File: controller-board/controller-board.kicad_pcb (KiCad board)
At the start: 2 copper layers, 130 x 115 mm, 152 parts, among them J1 Conn_01x02, J2 Conn_01x02, J3 Conn_01x02, J4 Conn_01x02, J5 Conn_01x03, J6 Conn_01x02, U1 CAT4201, U10 CAT4201, U11 CAT4201, U12 CAT4201, U13 CAT4201, U14 CAT4201, U15 CAT4201, U16 DGD0216, U2 PocketBeagle, U3 LTC3624, U4 CAT4201, U5 CAT4201, U6 CAT4201, U7 MCP4728, U8 ADS1015IRUGR, U9 ADS1015IRUGR

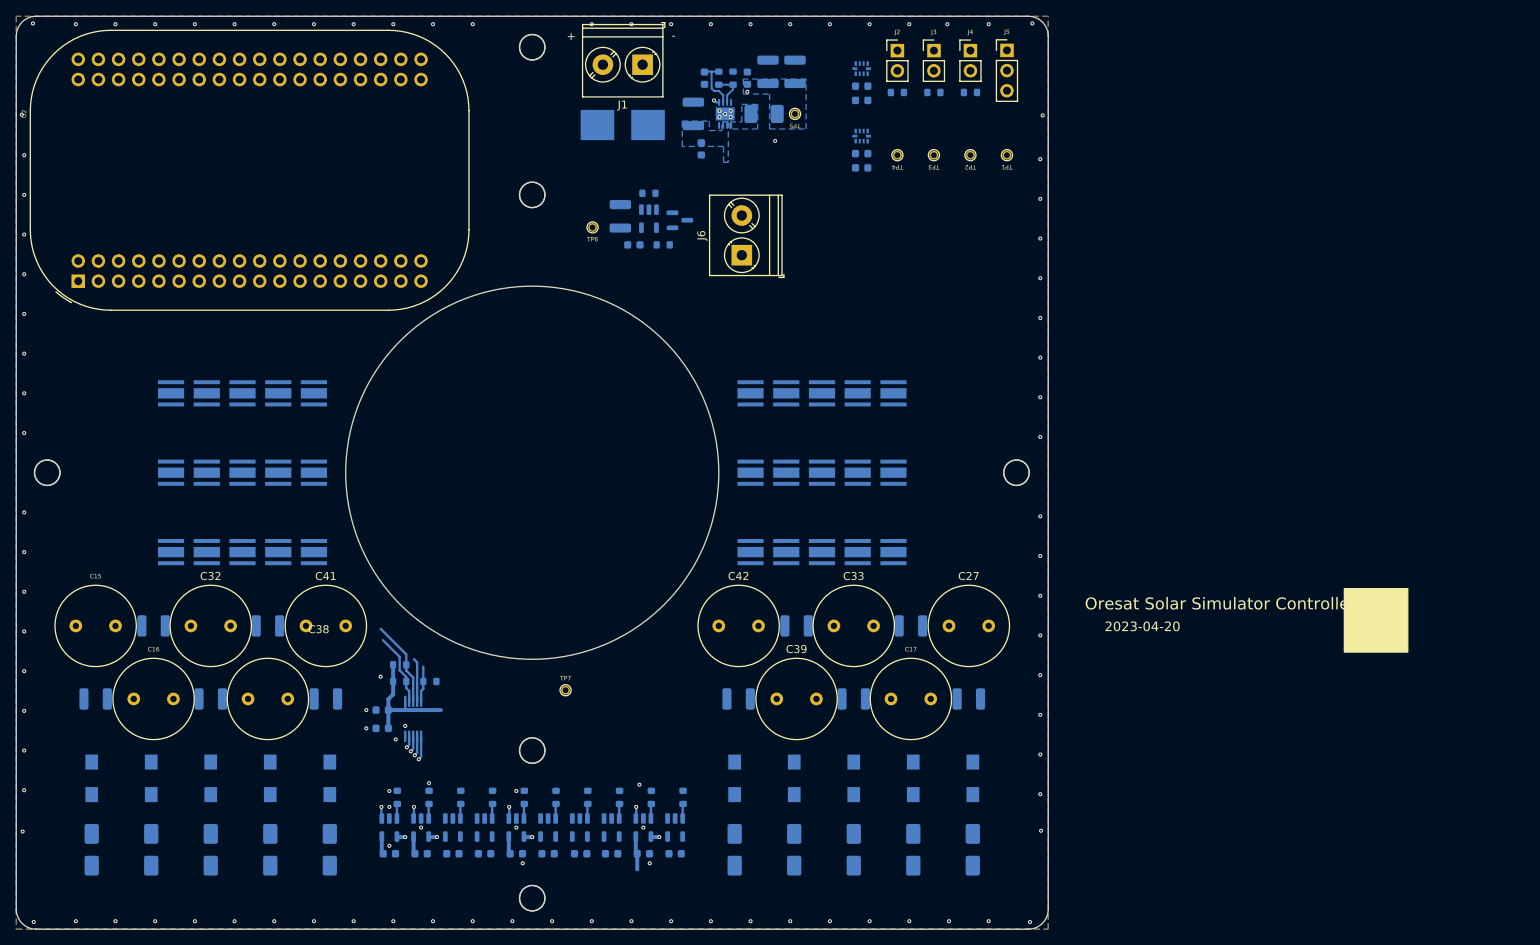
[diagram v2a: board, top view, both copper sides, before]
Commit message: Updated board design/layout and added step file
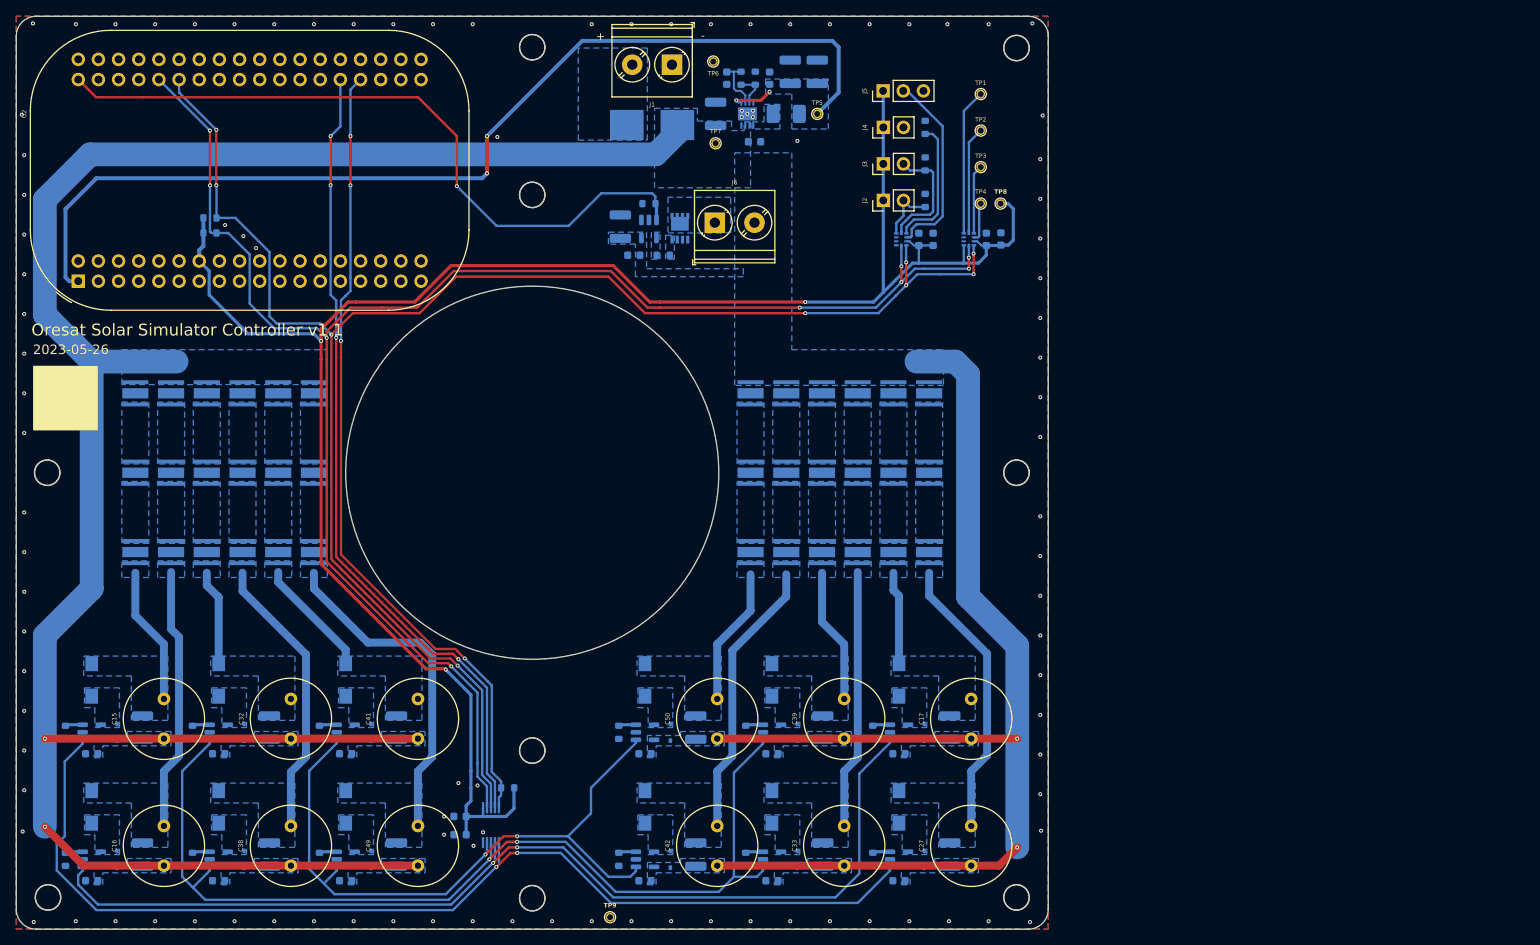
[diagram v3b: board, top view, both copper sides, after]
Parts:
- added C45: 4.7u, Capacitor_SMD:C_0603_1608Metric, B.Cu at (121.5, 153.9)
- added C46: 4.7u, Capacitor_SMD:C_0603_1608Metric, B.Cu at (159.2, 137.9)
- added C47: 22u, Capacitor_SMD:C_1210_3225Metric, B.Cu at (127.9, 150.6)
- added C48: 22u, Capacitor_SMD:C_1210_3225Metric, B.Cu at (165.6, 134.6)
- added C49: NP, Capacitor_THT:C_Radial_D10.0mm_H16.0mm_P5.00mm, F.Cu at (130.6, 152.0)
- added C50: NP, Capacitor_THT:C_Radial_D10.0mm_H16.0mm_P5.00mm, F.Cu at (168.3, 136.0)
- added D24: NSR0320, Diode_SMD:D_SOD-323, B.Cu at (124.7, 151.2)
- added D42: NSR0320, Diode_SMD:D_SOD-323, B.Cu at (162.4, 135.2)
- added D43: XPEBBL-L1-0000-00201, oresat-diodes:Cree-LED, B.Cu at (117.5, 92.5)
- added D44: XPEBBL-L1-0000-00201, oresat-diodes:Cree-LED, B.Cu at (117.5, 112.5)
- added D45: XPEBBL-L1-0000-00201, oresat-diodes:Cree-LED, B.Cu at (172.5, 92.5)
- added D46: XPEBBL-L1-0000-00201, oresat-diodes:Cree-LED, B.Cu at (172.5, 112.5)
- added D47: XPEBBL-L1-0000-00201, oresat-diodes:Cree-LED, B.Cu at (117.5, 102.5)
- added D48: XPEBBL-L1-0000-00201, oresat-diodes:Cree-LED, B.Cu at (172.5, 102.5)
- added L12: 56u, Inductor_SMD:L_Wuerth_HCI-5040, B.Cu at (121.5, 144.6)
- added L13: 56u, Inductor_SMD:L_Wuerth_HCI-5040, B.Cu at (159.2, 128.6)
- added R21: 10k, Resistor_SMD:R_0603_1608Metric, B.Cu at (118.2, 151.2)
- added R22: 10k, Resistor_SMD:R_0603_1608Metric, B.Cu at (155.9, 135.2)
- added REF**: MountingHole_3.2mm_M3, MountingHole:MountingHole_3.2mm_M3, F.Cu at (206.0, 49.0)
- added REF**: MountingHole_3.2mm_M3, MountingHole:MountingHole_3.2mm_M3, F.Cu at (84.0, 156.0)
- added REF**: MountingHole_3.2mm_M3, MountingHole:MountingHole_3.2mm_M3, F.Cu at (206.0, 156.0)
- added TP8: TestPoint-MinTH, oresat-misc:TestPoint-MinTH, F.Cu at (204.0, 68.6)
- added TP9: TestPoint-MinTH, oresat-misc:TestPoint-MinTH, F.Cu at (154.8, 158.5)
- added U17: CAT4201, Package_TO_SOT_SMD:TSOT-23-5, B.Cu at (121.5, 151.2)
- added U18: CAT4201, Package_TO_SOT_SMD:TSOT-23-5, B.Cu at (159.2, 135.2)
- D1, D15, D16, D17, D2, D3, D34, D35, D4, D7: value SS210A -> NSR0320; footprint Diode_SMD:D_SMA -> Diode_SMD:D_SOD-323
- D10, D11, D12, D13, D14, D18, D19, D20, D21, D22, D23, D25, D26, D27, D28, D29, D30, D31, D32, D33, D36, D37, D38, D39, D40, D41, D5, D6, D8, D9: footprint LED_SMD:LED_Cree-XP -> oresat-diodes:Cree-LED
- Q1: value ~ -> SQS460EN; footprint Package_TO_SOT_SMD:SOT-23 -> Package_SO:Vishay_PowerPAK_1212-8_Single
- moved TP7 71.4 mm to (168.1, 61.0)
- moved R13 61.3 mm to (104.4, 72.3)
- moved R12 61.2 mm to (104.4, 70.4)
- moved R3 46.5 mm to (86.2, 151.2), turned to -90 degrees
- moved R2 42.6 mm to (86.2, 135.2), turned to -90 degrees
- moved U4 41.7 mm to (89.5, 151.2), turned to 0 degrees
- moved C2 41.6 mm to (89.5, 153.9), turned to 180 degrees
- moved C11 39.6 mm to (89.5, 137.9), turned to 180 degrees
- moved U1 39.4 mm to (89.5, 135.2), turned to 0 degrees
- moved R18 38.6 mm to (102.2, 151.2), turned to -90 degrees
- moved R16 34.8 mm to (102.2, 135.2), turned to -90 degrees
- moved C3 34.6 mm to (191.2, 137.9), turned to 180 degrees
- moved U5 34.4 mm to (191.2, 135.2), turned to 0 degrees
- moved U13 33.7 mm to (105.5, 151.2), turned to 0 degrees
- moved C34 33.7 mm to (105.5, 153.9), turned to 180 degrees
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- renumbered U16 to Q2
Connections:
- Q1 pad 1: Net-(Q1-G) -> GND
- Q1 pad 3: Net-(J6-Pin_1) -> GND
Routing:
- net VCC: track 10.2 -> 420.6 mm, vias 0 -> 4
- net +3.3V: track 16.0 -> 247.7 mm, vias 0 -> 3
- net /SCL1: track 9.07 -> 210.9 mm, vias 0 -> 9
- net /SDA1: track 10.8 -> 210.7 mm, vias 0 -> 9
- net +5V: track 0.75 -> 134.6 mm, vias 2 -> 4
- net /RED_LIM: track 4.51 -> 135.8 mm
- net /GREEN_LIM: track 5.49 -> 129.9 mm, vias 3 -> 2
- net /BLUE_LIM: track 2.02 -> 124.7 mm, vias 1 -> 2
- net /DAC_RDY/~{BSY}: track 4.49 -> 102.7 mm, vias 0 -> 4
- net /DAC_~{LDAC}: track 5.47 -> 102.3 mm, vias 0 -> 4
- net Net-(Q2-IN): track 0.00 -> 88.9 mm, vias 0 -> 1
- net /UV_LIM: track 3.01 -> 86.1 mm
- net Net-(D44-K): track 0.00 -> 42.7 mm
- net Net-(D37-K): track 0.00 -> 36.0 mm
- net Net-(D26-K): track 0.00 -> 35.8 mm
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- added copper zone on B.Cu, net Net-(D1-A)
- added copper zone on B.Cu, net Net-(D10-A)
- added copper zone on B.Cu, net Net-(D10-K)
- added copper zone on B.Cu, net Net-(D11-K)
- added copper zone on B.Cu, net Net-(D12-A)
- added copper zone on B.Cu, net Net-(D12-K)
- added copper zone on B.Cu, net Net-(D13-A)
- added copper zone on B.Cu, net Net-(D15-A)
- added copper zone on B.Cu, net Net-(D16-A)
- added copper zone on B.Cu, net Net-(D17-A)
- added copper zone on B.Cu, net Net-(D18-K)
- added copper zone on B.Cu, net Net-(D19-A)
- added copper zone on B.Cu, net Net-(D19-K)
- added copper zone on B.Cu, net Net-(D2-A)
- added copper zone on B.Cu, net Net-(D20-K)
- added copper zone on B.Cu, net Net-(D21-A)
- added copper zone on B.Cu, net Net-(D21-K)
- added copper zone on B.Cu, net Net-(D24-A)
- added copper zone on B.Cu, net Net-(D25-K)
- added copper zone on B.Cu, net Net-(D26-A)
- added copper zone on B.Cu, net Net-(D26-K)
- added copper zone on B.Cu, net Net-(D28-K)
- added copper zone on B.Cu, net Net-(D29-A)
- added copper zone on B.Cu, net Net-(D29-K)
- added copper zone on B.Cu, net Net-(D3-A)
- added copper zone on B.Cu, net Net-(D30-K)
- added copper zone on B.Cu, net Net-(D31-A)
- added copper zone on B.Cu, net Net-(D31-K)
- added copper zone on B.Cu, net Net-(D34-A)
- added copper zone on B.Cu, net Net-(D35-A)
- added copper zone on B.Cu, net Net-(D36-K)
- added copper zone on B.Cu, net Net-(D37-A)
- added copper zone on B.Cu, net Net-(D37-K)
- added copper zone on B.Cu, net Net-(D38-K)
- added copper zone on B.Cu, net Net-(D39-A)
- added copper zone on B.Cu, net Net-(D39-K)
- added copper zone on B.Cu, net Net-(D4-A)
- added copper zone on B.Cu, net Net-(D42-A)
- added copper zone on B.Cu, net Net-(D43-K)
- added copper zone on B.Cu, net Net-(D44-A)
- added copper zone on B.Cu, net Net-(D44-K)
- added copper zone on B.Cu, net Net-(D45-K)
- added copper zone on B.Cu, net Net-(D46-A)
- added copper zone on B.Cu, net Net-(D46-K)
- added copper zone on B.Cu, net Net-(D5-K)
- added copper zone on B.Cu, net Net-(D6-K)
- added copper zone on B.Cu, net Net-(D7-A)
- added copper zone on B.Cu, net Net-(D8-K)
- added copper zone on B.Cu, net Net-(J1-Pin_2)
- added copper zone on B.Cu, net Net-(J6-Pin_1)
- added copper zone on B.Cu, net Net-(Q1-G)
- added copper zone on B.Cu, net Net-(Q2-OUT)
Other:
- outline, holes or cut-outs redrawn
- board text added: "2023-05-26"
- board text added: "Oresat Solar Simulator Controller v1.1"
- board text removed: "2023-04-20"
- board text removed: "Oresat Solar Simulator Controller v1.0"

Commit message: Added GND stitching vias and on/off switch
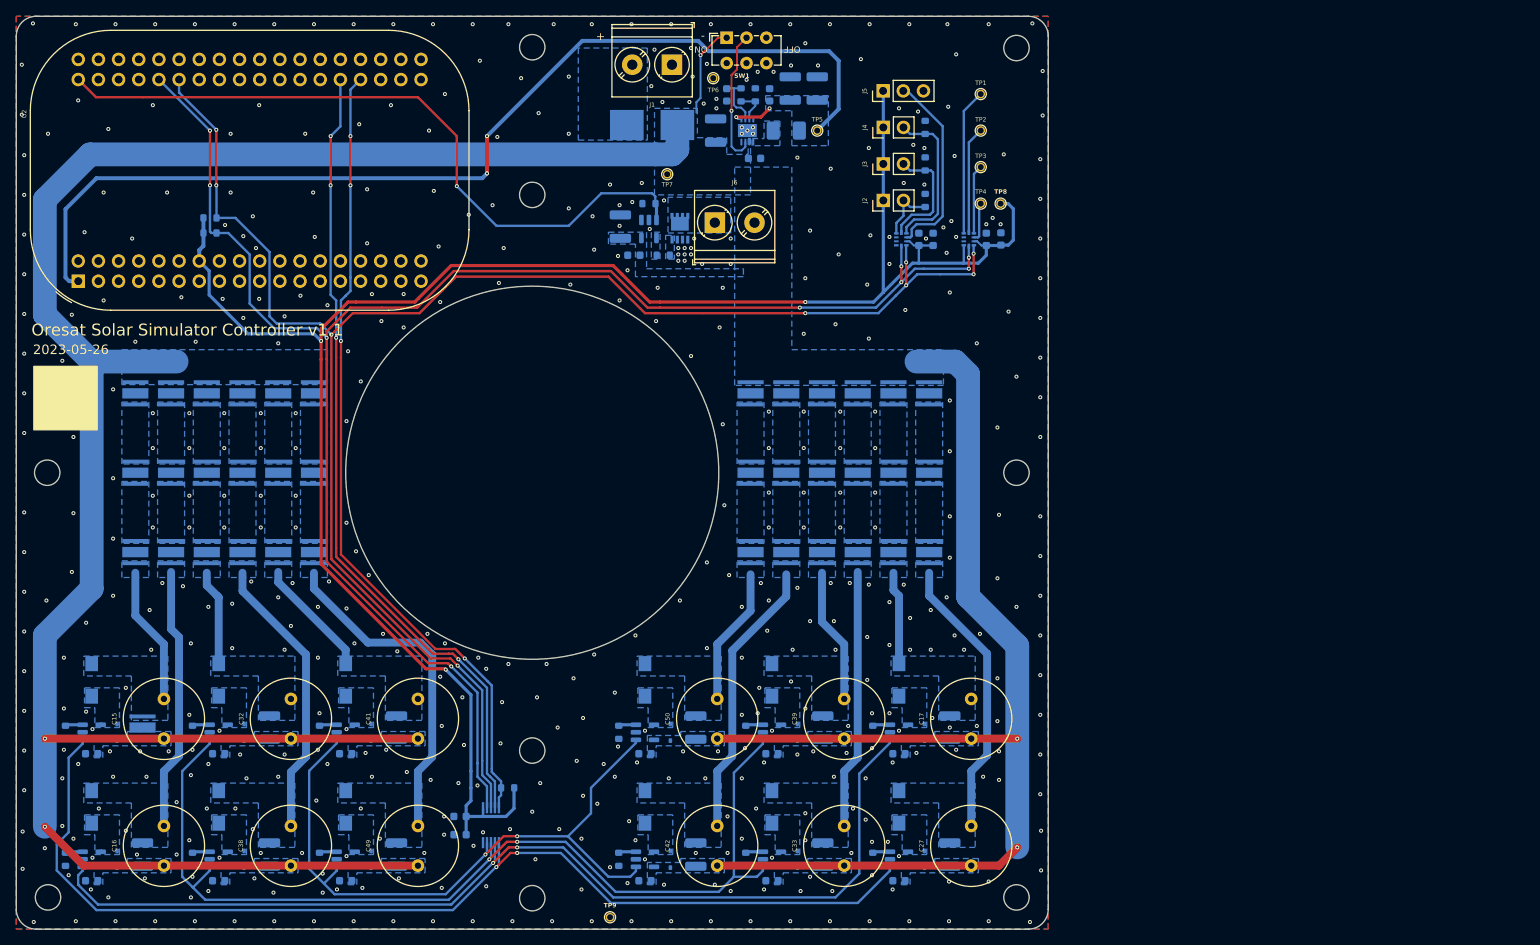
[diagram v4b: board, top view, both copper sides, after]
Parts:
- added SW1: EG1271, Button_Switch_THT:SW_E-Switch_EG1271_SPDT, F.Cu at (169.5, 47.7)
- C1: footprint Capacitor_SMD:C_1210_3225Metric -> oresat-diodes:Cree-LED
- moved TP7 7.24 mm to (162.0, 64.9)
- moved C10 2.10 mm to (169.5, 54.9)
- moved C5 2.10 mm to (168.1, 59.4)
- moved C6 2.10 mm to (173.0, 62.9)
- moved C7 2.10 mm to (177.5, 54.1)
- moved C8 2.10 mm to (180.9, 54.1)
- moved C9 2.10 mm to (174.9, 54.9)
- moved L5 2.10 mm to (177.0, 59.4)
- moved R8 2.10 mm to (171.3, 54.9)
- moved R9 2.10 mm to (173.1, 54.9)
- moved TP5 2.10 mm to (180.9, 59.4)
- moved U3 2.10 mm to (172.1, 59.4)
- moved TP6 2.10 mm to (167.8, 52.8)
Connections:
- U3 pad 3: VCC -> Net-(SW1-B)
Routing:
- net Net-(SW1-B): track 0.00 -> 17.2 mm, vias 0 -> 1
- net VCC: track 420.6 -> 431.4 mm, vias 4 -> 5
- net /THERM3: track 16.7 -> 19.8 mm
- net +5V: track 134.6 -> 135.7 mm
- net GND: vias 102 -> 518
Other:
- outline, holes or cut-outs redrawn
- board text added: "OFF"
- board text added: "ON"

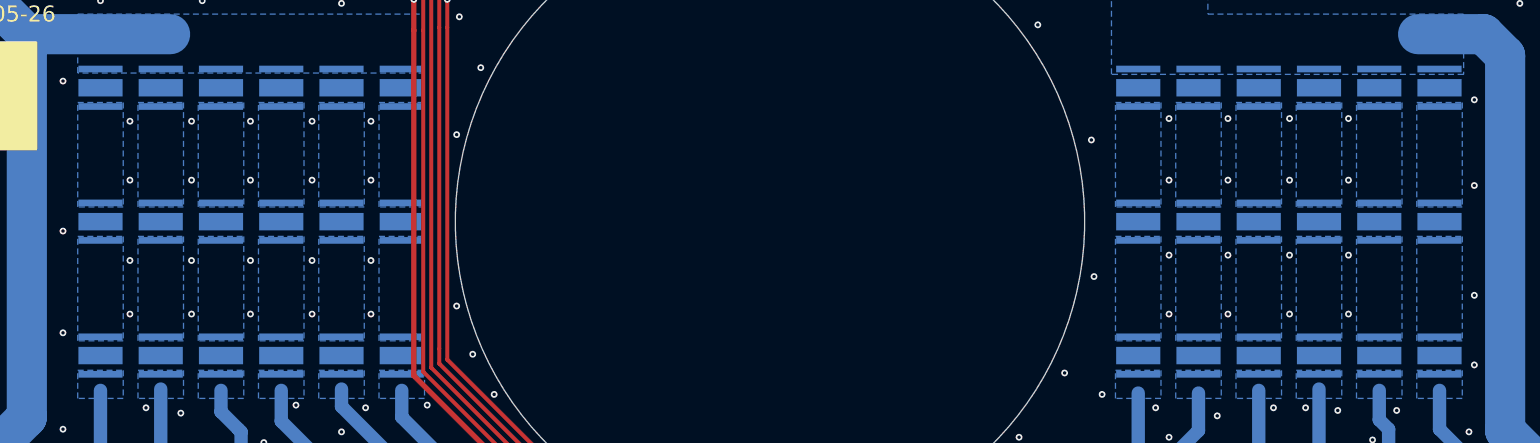
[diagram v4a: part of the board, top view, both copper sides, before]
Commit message: Added thermal vias for LEDS and soldermask openings to bypass the LEDs
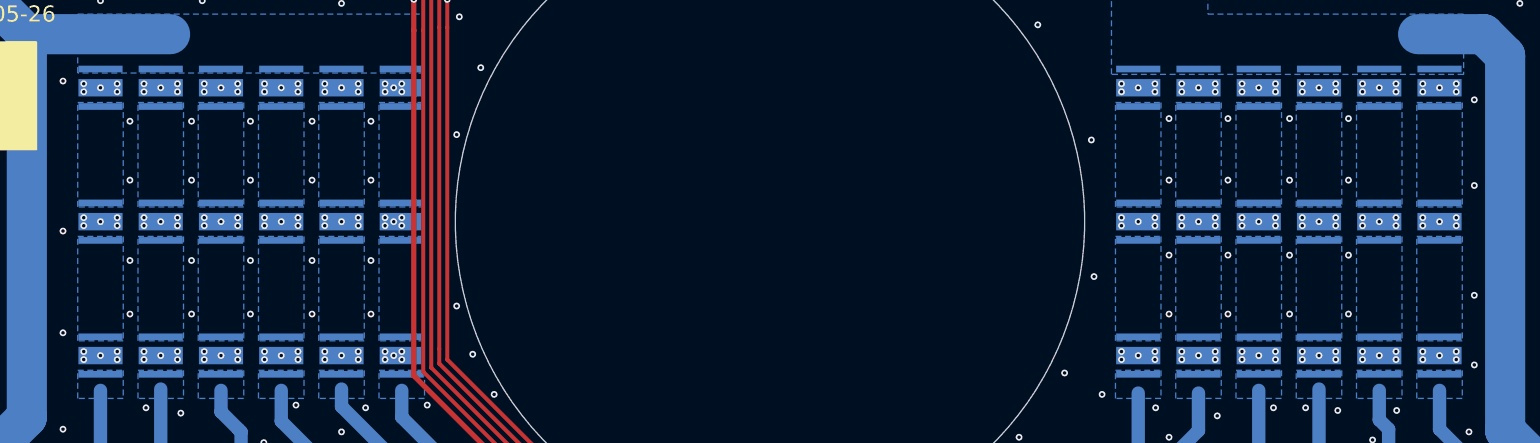
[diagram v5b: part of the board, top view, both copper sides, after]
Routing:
- net GND: vias 518 -> 698
